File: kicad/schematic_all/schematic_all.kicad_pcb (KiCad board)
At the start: 2 copper layers, 88.9 x 88.9 mm, 42 parts, among them SW1 Button 1, SW2 Encoder 1, SW3 Button 2, SW4 Encoder 2, SW5 Button 3, U1 L7805, U2 RPi_Pico, U3 RDA5807M_Module, U4 LM386

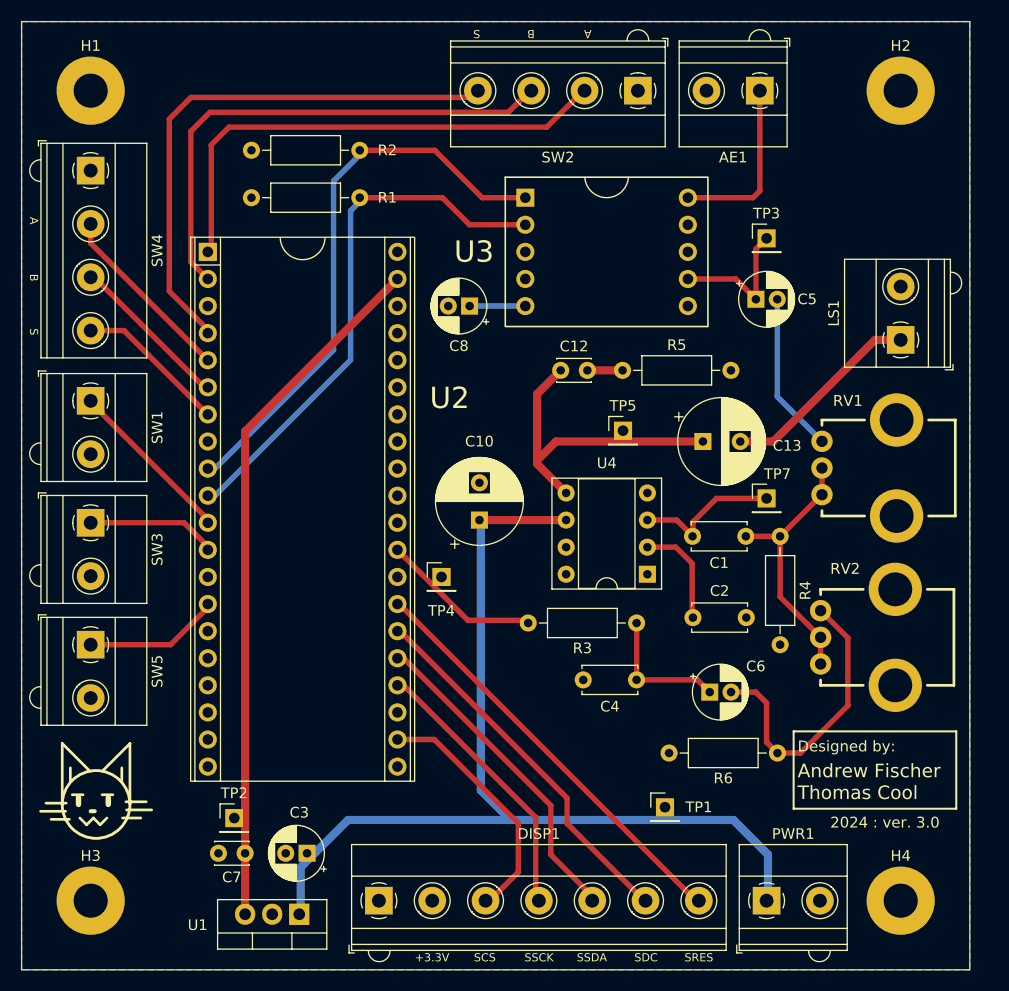
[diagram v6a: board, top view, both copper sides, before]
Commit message: fix pico power issues
swap regulator caps to match L4941 spec
add +5V pinout
add diode to prevent backfeeding from pico
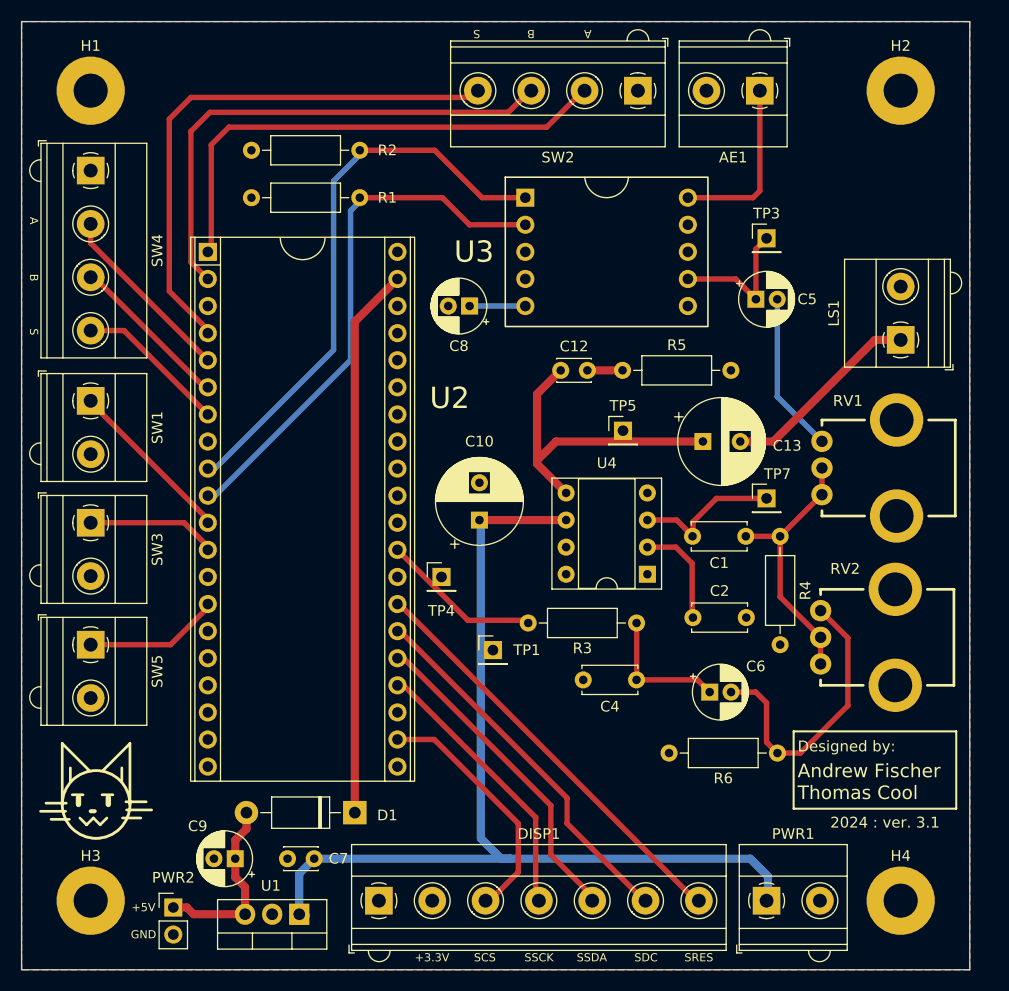
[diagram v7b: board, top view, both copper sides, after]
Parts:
- removed C3: 220nF, Capacitor_THT:CP_Radial_D5.0mm_P2.00mm
- removed TP2: TestPoint, Connector_PinHeader_2.54mm:PinHeader_1x01_P2.54mm_Vertical
- added C9: 22uF, Capacitor_THT:CP_Radial_D5.0mm_P2.00mm, F.Cu at (77.2, 116.6)
- added D1: 1N4007, Diode_THT:D_DO-41_SOD81_P10.16mm_Horizontal, F.Cu at (88.4, 112.3)
- added PWR2: Power Out, Connector_PinHeader_2.54mm:PinHeader_1x02_P2.54mm_Vertical, F.Cu at (71.4, 121.2)
- moved TP1 21.8 mm to (101.3, 97.0)
- moved C7 6.50 mm to (84.6, 116.6)
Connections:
- C7 pad 1: +5V -> +12V
- RV1 pad 4: (no net) -> GND
- RV1 pad 5: (no net) -> GND
- RV2 pad 4: (no net) -> GND
- RV2 pad 5: (no net) -> GND
- U2 pad 39: +5V -> Net-(D1-K)
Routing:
- net Net-(D1-K): track 0.00 -> 51.7 mm
- net +5V: track 65.5 -> 17.3 mm
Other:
- board text added: "+5V"
- board text added: "2024 : ver. 3.1"
- board text added: "GND"
- board text removed: "2024 : ver. 3.0"

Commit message: add trace and jumper between radio output and pico ADC
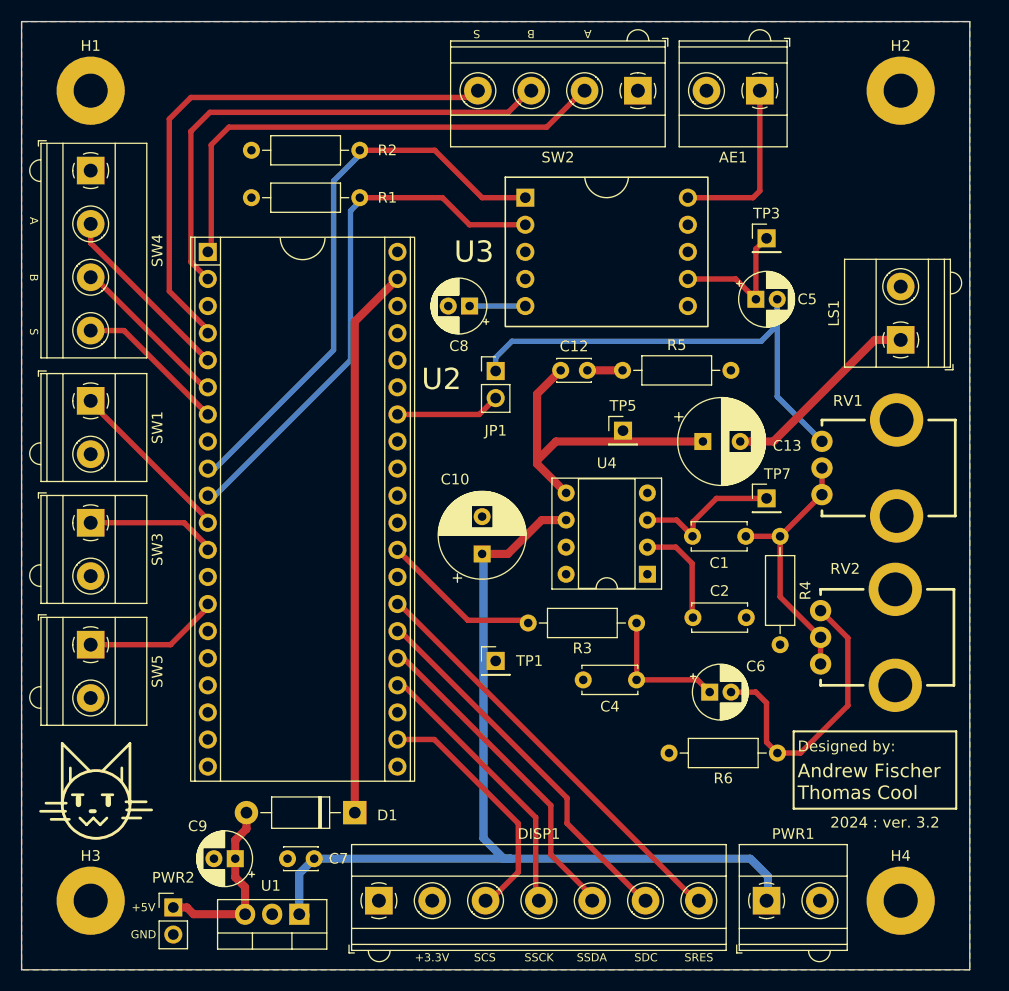
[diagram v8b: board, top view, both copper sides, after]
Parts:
- removed TP4: TestPoint, Connector_PinHeader_2.54mm:PinHeader_1x01_P2.54mm_Vertical
- added JP1: ADCJumper, Connector_PinHeader_2.54mm:PinHeader_1x02_P2.54mm_Vertical, F.Cu at (101.6, 70.9)
- moved C10 3.19 mm to (100.3, 88.0)
- moved TP1 1.05 mm to (101.6, 98.0)
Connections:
- U2 pad 34: unconnected-(U2-GP28/ADC2-Pad34) -> /ADC
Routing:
- net Net-(JP1-A): track 15.1 -> 46.4 mm
- net /ADC: track 0.00 -> 9.84 mm
- net +12V: track 94.0 -> 91.4 mm
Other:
- board text added: "2024 : ver. 3.2"
- board text removed: "2024 : ver. 3.1"
